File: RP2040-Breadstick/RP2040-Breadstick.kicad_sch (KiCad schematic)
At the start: 22 parts, among them J111 Conn_01x01, J112 Conn_01x01, J113 Conn_01x01, J114 Conn_01x01, J115 Conn_01x01, J116 Conn_01x01, J117 Conn_01x01, J118 Conn_01x01, J119 Conn_01x01, J120 Conn_01x02, J121 Conn_01x01, J122 Conn_01x01, J123 Conn_01x01, J124 Conn_01x01, J125 Conn_01x01, J126 Conn_01x01, J127 Conn_01x01, J128 Conn_01x01, J129 Conn_01x01, J130 Conn_01x02, J501 Conn_01x05, J502 Conn_01x05

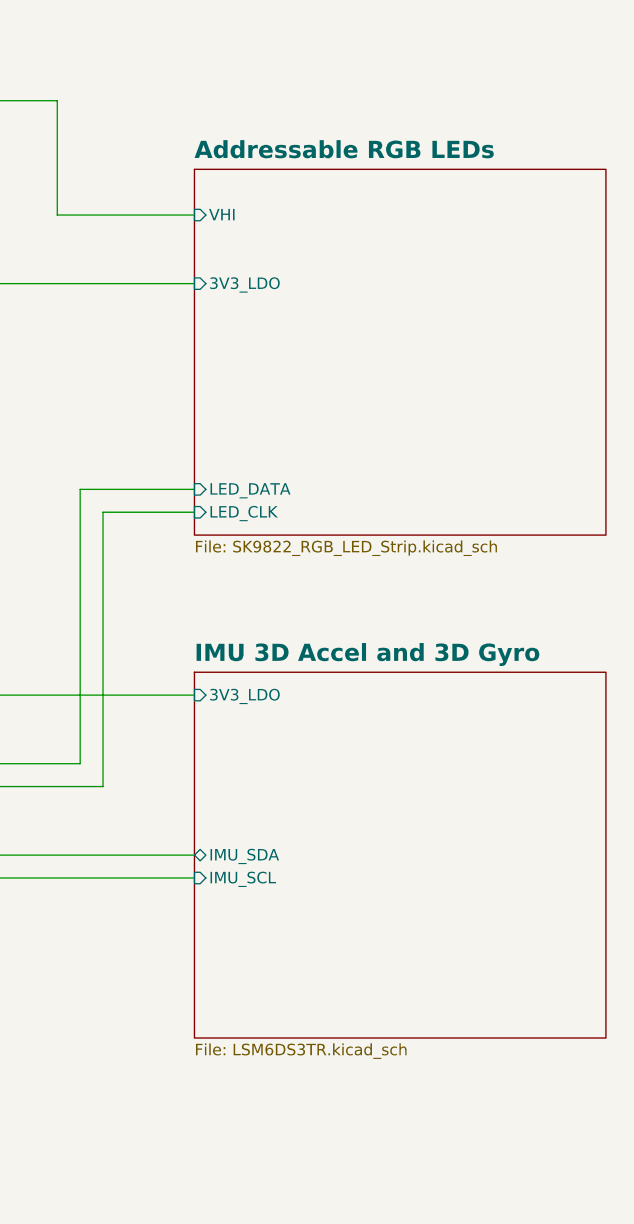
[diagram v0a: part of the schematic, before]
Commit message: deleted leds and imu in schematic
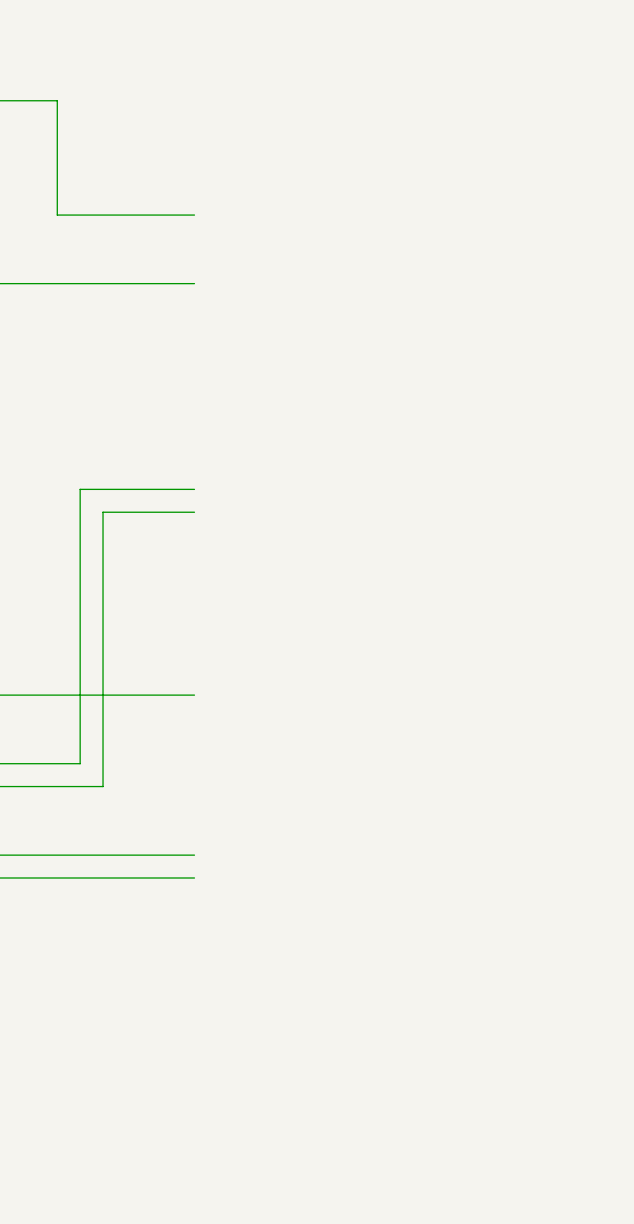
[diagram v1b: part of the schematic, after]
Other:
- removed sheet Addressable RGB LEDs
- removed sheet IMU 3D Accel and 3D Gyro
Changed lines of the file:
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@@
     (pin "1")
     (instances
-      (project "pcb2blender_tmp"
+      (project "RP2040-Breadstick"
         (path "/c1b11207-7c0a-49b3-a41d-2fe677d5f3b8"
           (reference "J124") (unit 1)
@@
     (pin "1")
     (instances
-      (project "pcb2blender_tmp"
+      (project "RP2040-Breadstick"
         (path "/c1b11207-7c0a-49b3-a41d-2fe677d5f3b8"
           (reference "#PWR0509") (unit 1)
@@
     (pin "2")
     (instances
-      (project "pcb2blender_tmp"
+      (project "RP2040-Breadstick"
         (path "/c1b11207-7c0a-49b3-a41d-2fe677d5f3b8"
           (reference "J130") (unit 1)
@@
     (pin "1")
     (instances
-      (project "pcb2blender_tmp"
+      (project "RP2040-Breadstick"
         (path "/c1b11207-7c0a-49b3-a41d-2fe677d5f3b8"
           (reference "J115") (unit 1)
@@
     (pin "2")
     (instances
-      (project "pcb2blender_tmp"
+      (project "RP2040-Breadstick"
         (path "/c1b11207-7c0a-49b3-a41d-2fe677d5f3b8"
           (reference "J120") (unit 1)
@@
     (pin "1")
     (instances
-      (project "pcb2blender_tmp"
+      (project "RP2040-Breadstick"
         (path "/c1b11207-7c0a-49b3-a41d-2fe677d5f3b8"
           (reference "J117") (unit 1)
@@
     (pin "1")
     (instances
-      (project "pcb2blender_tmp"
+      (project "RP2040-Breadstick"
         (path "/c1b11207-7c0a-49b3-a41d-2fe677d5f3b8"
           (reference "J111") (unit 1)
@@
     (pin "1")
     (instances
-      (project "pcb2blender_tmp"
+      (project "RP2040-Breadstick"
         (path "/c1b11207-7c0a-49b3-a41d-2fe677d5f3b8"
           (reference "J116") (unit 1)
@@
     (pin "1")
     (instances
-      (project "pcb2blender_tmp"
+      (project "RP2040-Breadstick"
         (path "/c1b11207-7c0a-49b3-a41d-2fe677d5f3b8"
           (reference "J125") (unit 1)
@@
     (pin "1")
     (instances
-      (project "pcb2blender_tmp"
+      (project "RP2040-Breadstick"
         (path "/c1b11207-7c0a-49b3-a41d-2fe677d5f3b8"
           (reference "J114") (unit 1)
@@
     (pin "1")
     (instances
-      (project "pcb2blender_tmp"
+      (project "RP2040-Breadstick"
         (path "/c1b11207-7c0a-49b3-a41d-2fe677d5f3b8"
           (reference "J119") (unit 1)
@@
     (pin "5")
     (instances
-      (project "pcb2blender_tmp"
+      (project "RP2040-Breadstick"
         (path "/c1b11207-7c0a-49b3-a41d-2fe677d5f3b8"
           (reference "J502") (unit 1)
@@
     (pin "1")
     (instances
-      (project "pcb2blender_tmp"
+      (project "RP2040-Breadstick"
         (path "/c1b11207-7c0a-49b3-a41d-2fe677d5f3b8"
           (reference "J122") (unit 1)
@@
     (pin "1")
     (instances
-      (project "pcb2blender_tmp"
+      (project "RP2040-Breadstick"
         (path "/c1b11207-7c0a-49b3-a41d-2fe677d5f3b8"
           (reference "J112") (unit 1)
@@
     (pin "1")
     (instances
-      (project "pcb2blender_tmp"
+      (project "RP2040-Breadstick"
         (path "/c1b11207-7c0a-49b3-a41d-2fe677d5f3b8"
           (reference "J127") (unit 1)
@@
     (pin "5")
     (instances
-      (project "pcb2blender_tmp"
+      (project "RP2040-Breadstick"
         (path "/c1b11207-7c0a-49b3-a41d-2fe677d5f3b8"
           (reference "J501") (unit 1)
@@
     (pin "1")
     (instances
-      (project "pcb2blender_tmp"
+      (project "RP2040-Breadstick"
         (path "/c1b11207-7c0a-49b3-a41d-2fe677d5f3b8"
           (reference "J118") (unit 1)
@@
     (pin "1")
     (instances
-      (project "pcb2blender_tmp"
+      (project "RP2040-Breadstick"
         (path "/c1b11207-7c0a-49b3-a41d-2fe677d5f3b8"
           (reference "J123") (unit 1)
@@
     (pin "1")
     (instances
-      (project "pcb2blender_tmp"
+      (project "RP2040-Breadstick"
         (path "/c1b11207-7c0a-49b3-a41d-2fe677d5f3b8"
           (reference "J121") (unit 1)
@@
     (pin "1")
     (instances
-      (project "pcb2blender_tmp"
+      (project "RP2040-Breadstick"
         (path "/c1b11207-7c0a-49b3-a41d-2fe677d5f3b8"
           (reference "J128") (unit 1)
@@
     (pin "1")
     (instances
-      (project "pcb2blender_tmp"
+      (project "RP2040-Breadstick"
         (path "/c1b11207-7c0a-49b3-a41d-2fe677d5f3b8"
           (reference "J113") (unit 1)
@@
     (pin "1")
     (instances
-      (project "pcb2blender_tmp"
+      (project "RP2040-Breadstick"
         (path "/c1b11207-7c0a-49b3-a41d-2fe677d5f3b8"
           (reference "#PWR0508") (unit 1)
@@
     (pin "1")
     (instances
-      (project "pcb2blender_tmp"
+      (project "RP2040-Breadstick"
         (path "/c1b11207-7c0a-49b3-a41d-2fe677d5f3b8"
           (reference "J129") (unit 1)
@@
     (pin "1")
     (instances
-      (project "pcb2blender_tmp"
+      (project "RP2040-Breadstick"
         (path "/c1b11207-7c0a-49b3-a41d-2fe677d5f3b8"
           (reference "J126") (unit 1)
@@
     (pin "1")
     (instances
-      (project "pcb2blender_tmp"
+      (project "RP2040-Breadstick"
         (path "/c1b11207-7c0a-49b3-a41d-2fe677d5f3b8"
           (reference "#PWR0103") (unit 1)
@@
     )
     (instances
-      (project "pcb2blender_tmp"
+      (project "RP2040-Breadstick"
         (path "/c1b11207-7c0a-49b3-a41d-2fe677d5f3b8" (page "2"))
       )
@@
     )
     (instances
-      (project "pcb2blender_tmp"
+      (project "RP2040-Breadstick"
         (path "/c1b11207-7c0a-49b3-a41d-2fe677d5f3b8" (page "5"))
-      )
-    )
-  )
-  (sheet (at 198.12 31.75) (size 45.72 40.64) (fields_autoplaced)
-    (stroke (width 0.1524) (type solid))
-    (fill (color 0 0 0 0.0000))
-    (property "Sheetname" "Addressable RGB LEDs" (at 198.12 30.7209 0)
-      (effects (font (size 1.905 1.905) bold) (justify left bottom))
-    )
-    (property "Sheetfile" "SK9822_RGB_LED_Strip.kicad_sch" (at 198.12 72.9746 0)
-      (effects (font (size 1.27 1.27)) (justify left top))
-    )
-    (pin "VHI" input (at 198.12 36.83 180)
-      (effects (font (size 1.27 1.27)) (justify left))
-    )
-    (pin "3V3_LDO" input (at 198.12 44.45 180)
-      (effects (font (size 1.27 1.27)) (justify left))
-    )
-    (pin "LED_CLK" input (at 198.12 69.85 180)
-      (effects (font (size 1.27 1.27)) (justify left))
-    )
-    (pin "LED_DATA" input (at 198.12 67.31 180)
-      (effects (font (size 1.27 1.27)) (justify left))
-    )
-    (instances
-      (project "pcb2blender_tmp"
-        (path "/c1b11207-7c0a-49b3-a41d-2fe677d5f3b8" (page "3"))
-      )
-    )
-  )
-  (sheet (at 198.12 87.63) (size 45.72 40.64) (fields_autoplaced)
-    (stroke (width 0.1524) (type solid))
-    (fill (color 0 0 0 0.0000))
-    (property "Sheetname" "IMU 3D Accel and 3D Gyro" (at 198.12 86.6009 0)
-      (effects (font (size 1.905 1.905) bold) (justify left bottom))
-    )
-    (property "Sheetfile" "LSM6DS3TR.kicad_sch" (at 198.12 128.8546 0)
-      (effects (font (size 1.27 1.27)) (justify left top))
-    )
-    (pin "IMU_SDA" bidirectional (at 198.12 107.95 180)
-      (effects (font (size 1.27 1.27)) (justify left))
-    )
-    (pin "IMU_SCL" input (at 198.12 110.49 180)
-      (effects (font (size 1.27 1.27)) (justify left))
-    )
-    (pin "3V3_LDO" input (at 198.12 90.17 180)
-      (effects (font (size 1.27 1.27)) (justify left))
-    )
-    (instances
-      (project "pcb2blender_tmp"
-        (path "/c1b11207-7c0a-49b3-a41d-2fe677d5f3b8" (page "4"))
       )
     )
@@
     )
     (instances
-      (project "pcb2blender_tmp"
+      (project "RP2040-Breadstick"
         (path "/c1b11207-7c0a-49b3-a41d-2fe677d5f3b8" (page "6"))
       )

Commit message: cleaned up unused tracks/vias
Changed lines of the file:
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@@
     (comment 5 "https://shop.breadstick.ca/")
   )
-  (junction (at 173.99 44.45) (diameter 0) (color 0 0 0 0)
-  )
   (junction (at 139.7 69.85) (diameter 0) (color 0 0 0 0)
-  )
-  (junction (at 173.99 90.17) (diameter 0) (color 0 0 0 0)
   )
   (wire (pts (xy 102.87 31.75) (xy 102.87 44.45))
@@
   )
   (wire (pts (xy 109.22 140.97) (xy 111.76 140.97))
-    (stroke (width 0) (type default))
-  )
-  (wire (pts (xy 182.88 36.83) (xy 198.12 36.83))
     (stroke (width 0) (type default))
   )
@@
     (stroke (width 0) (type default))
   )
-  (wire (pts (xy 173.99 44.45) (xy 173.99 90.17))
-    (stroke (width 0) (type default))
-  )
-  (wire (pts (xy 157.48 110.49) (xy 198.12 110.49))
-    (stroke (width 0) (type default))
-  )
-  (wire (pts (xy 157.48 107.95) (xy 198.12 107.95))
+  (wire (pts (xy 173.99 31.75) (xy 173.99 90.17))
     (stroke (width 0) (type default))
   )
@@
     (stroke (width 0) (type default))
   )
-  (wire (pts (xy 182.88 24.13) (xy 182.88 36.83))
-    (stroke (width 0) (type default))
-  )
   (wire (pts (xy 124.46 64.77) (xy 142.24 64.77))
     (stroke (width 0) (type default))
   )
-  (wire (pts (xy 173.99 44.45) (xy 198.12 44.45))
-    (stroke (width 0) (type default))
-  )
   (wire (pts (xy 157.48 140.97) (xy 160.02 140.97))
-    (stroke (width 0) (type default))
-  )
-  (wire (pts (xy 187.96 69.85) (xy 198.12 69.85))
     (stroke (width 0) (type default))
   )
@@
     (stroke (width 0) (type default))
   )
-  (wire (pts (xy 173.99 31.75) (xy 173.99 44.45))
-    (stroke (width 0) (type default))
-  )
   (wire (pts (xy 106.68 24.13) (xy 111.76 24.13))
     (stroke (width 0) (type default))
@@
     (stroke (width 0) (type default))
   )
-  (wire (pts (xy 157.48 24.13) (xy 182.88 24.13))
-    (stroke (width 0) (type default))
-  )
   (wire (pts (xy 157.48 90.17) (xy 173.99 90.17))
     (stroke (width 0) (type default))
   )
   (wire (pts (xy 102.87 90.17) (xy 111.76 90.17))
-    (stroke (width 0) (type default))
-  )
-  (wire (pts (xy 173.99 90.17) (xy 198.12 90.17))
-    (stroke (width 0) (type default))
-  )
-  (wire (pts (xy 157.48 100.33) (xy 187.96 100.33))
     (stroke (width 0) (type default))
   )
@@
     (stroke (width 0) (type default))
   )
-  (wire (pts (xy 157.48 97.79) (xy 185.42 97.79))
-    (stroke (width 0) (type default))
-  )
   (wire (pts (xy 111.76 121.92) (xy 109.22 121.92))
     (stroke (width 0) (type default))
   )
   (wire (pts (xy 81.28 44.45) (xy 102.87 44.45))
-    (stroke (width 0) (type default))
-  )
-  (wire (pts (xy 185.42 67.31) (xy 198.12 67.31))
     (stroke (width 0) (type default))
   )
@@
     (stroke (width 0) (type default))
   )
-  (wire (pts (xy 187.96 100.33) (xy 187.96 69.85))
-    (stroke (width 0) (type default))
-  )
   (wire (pts (xy 81.28 69.85) (xy 86.36 69.85))
     (stroke (width 0) (type default))
@@
     (stroke (width 0) (type default))
   )
-  (wire (pts (xy 185.42 97.79) (xy 185.42 67.31))
-    (stroke (width 0) (type default))
-  )
